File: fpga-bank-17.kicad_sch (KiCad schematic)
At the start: 1 part, among them U1 XC7K410T-2FFG900I

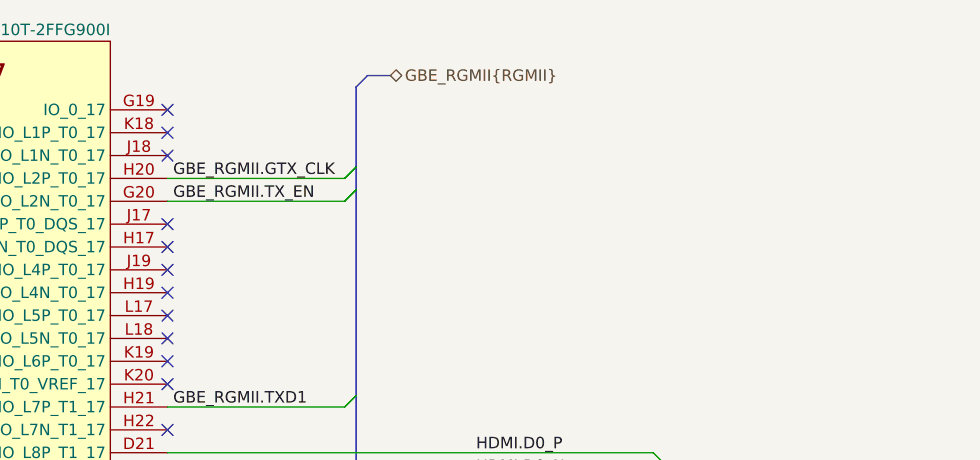
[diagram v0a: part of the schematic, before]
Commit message: Added control signals on FMC connector
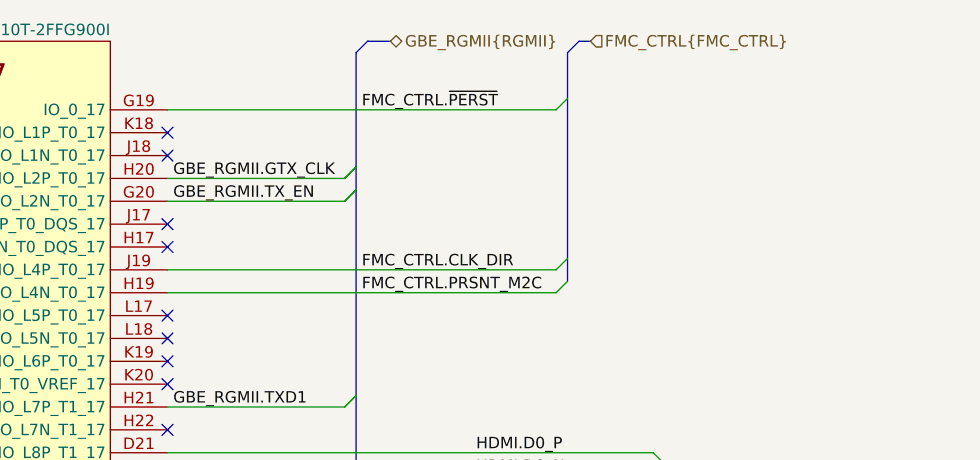
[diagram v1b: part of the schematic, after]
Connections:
- net FMC_CTRL.~{PERST}: now reaches U1.G19 (IO_0_17)
- net FMC_CTRL.PRSNT_M2C: now reaches U1.H19 (IO_L4N_T0_17)
- net FMC_CTRL.CLK_DIR: now reaches U1.J19 (IO_L4P_T0_17)
- no-connect marks 18 -> 15
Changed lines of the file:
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@@
   (no_connect (at 143.51 109.22))
   (no_connect (at 143.51 99.06))
-  (no_connect (at 143.51 101.6))
-  (no_connect (at 143.51 104.14))
   (no_connect (at 143.51 106.68))
   (no_connect (at 143.51 96.52))
-  (no_connect (at 143.51 83.82))
   (no_connect (at 143.51 86.36))
   (no_connect (at 143.51 88.9))
@@
     (stroke (width 0) (type default) (color 0 0 0 0))
   )
+  (bus_entry (at 187.96 82.55) (size -1.27 1.27)
+    (stroke (width 0) (type default) (color 0 0 0 0))
+  )
   (bus_entry (at 164.465 133.35) (size -1.27 1.27)
     (stroke (width 0) (type default) (color 0 0 0 0))
@@
     (stroke (width 0) (type default) (color 0 0 0 0))
   )
+  (bus_entry (at 187.96 102.87) (size -1.27 1.27)
+    (stroke (width 0) (type default) (color 0 0 0 0))
+  )
   (bus_entry (at 231.14 166.37) (size -1.27 1.27)
     (stroke (width 0) (type default) (color 0 0 0 0))
@@
     (stroke (width 0) (type default) (color 0 0 0 0))
   )
+  (bus_entry (at 187.96 100.33) (size -1.27 1.27)
+    (stroke (width 0) (type default) (color 0 0 0 0))
+  )
   (bus_entry (at 197.485 177.8) (size 1.27 1.27)
     (stroke (width 0) (type default) (color 0 0 0 0))
@@
     (stroke (width 0) (type default) (color 0 0 0 0))
   )
-  (bus (pts (xy 164.465 81.28) (xy 164.465 90.17))
-    (stroke (width 0) (type default) (color 0 0 0 0))
-  )
-  (bus (pts (xy 168.275 80.01) (xy 165.735 80.01))
+  (bus (pts (xy 187.96 82.55) (xy 187.96 100.33))
+    (stroke (width 0) (type default) (color 0 0 0 0))
+  )
+  (bus (pts (xy 164.465 77.47) (xy 164.465 90.17))
+    (stroke (width 0) (type default) (color 0 0 0 0))
+  )
+  (bus (pts (xy 168.275 76.2) (xy 165.735 76.2))
     (stroke (width 0) (type default) (color 0 0 0 0))
   )
@@
     (stroke (width 0) (type default) (color 0 0 0 0))
   )
-  (bus (pts (xy 164.465 81.28) (xy 165.735 80.01))
+  (bus (pts (xy 164.465 77.47) (xy 165.735 76.2))
+    (stroke (width 0) (type default) (color 0 0 0 0))
+  )
+  (wire (pts (xy 143.51 83.82) (xy 186.69 83.82))
     (stroke (width 0) (type default) (color 0 0 0 0))
   )
@@
     (stroke (width 0) (type default) (color 0 0 0 0))
   )
+  (bus (pts (xy 190.5 76.2) (xy 189.23 76.2))
+    (stroke (width 0) (type default) (color 0 0 0 0))
+  )
   (wire (pts (xy 143.51 185.42) (xy 229.87 185.42))
     (stroke (width 0) (type default) (color 0 0 0 0))
@@
     (stroke (width 0) (type default) (color 0 0 0 0))
   )
+  (bus (pts (xy 187.96 100.33) (xy 187.96 102.87))
+    (stroke (width 0) (type default) (color 0 0 0 0))
+  )
   (wire (pts (xy 143.51 195.58) (xy 229.87 195.58))
     (stroke (width 0) (type default) (color 0 0 0 0))
@@
     (stroke (width 0) (type default) (color 0 0 0 0))
   )
+  (bus (pts (xy 187.96 77.47) (xy 187.96 82.55))
+    (stroke (width 0) (type default) (color 0 0 0 0))
+  )
+  (bus (pts (xy 187.96 77.47) (xy 189.23 76.2))
+    (stroke (width 0) (type default) (color 0 0 0 0))
+  )
   (bus (pts (xy 198.755 207.01) (xy 198.755 208.915))
     (stroke (width 0) (type default) (color 0 0 0 0))
@@
     (stroke (width 0) (type default) (color 0 0 0 0))
   )
+  (wire (pts (xy 143.51 104.14) (xy 186.69 104.14))
+    (stroke (width 0) (type default) (color 0 0 0 0))
+  )
   (wire (pts (xy 197.485 203.2) (xy 143.51 203.2))
     (stroke (width 0) (type default) (color 0 0 0 0))
@@
   )
   (wire (pts (xy 143.51 170.18) (xy 229.87 170.18))
+    (stroke (width 0) (type default) (color 0 0 0 0))
+  )
+  (wire (pts (xy 143.51 101.6) (xy 186.69 101.6))
     (stroke (width 0) (type default) (color 0 0 0 0))
   )
@@
     (effects (font (size 1.27 1.27)) (justify left bottom))
   )
+  (label "FMC_CTRL.PRSNT_M2C" (at 165.1 104.14 0)
+    (effects (font (size 1.27 1.27)) (justify left bottom))
+  )
   (label "HDMI.D2_N" (at 177.8 205.74 0)
     (effects (font (size 1.27 1.27)) (justify left bottom))
@@
     (effects (font (size 1.27 1.27)) (justify left bottom))
   )
+  (label "FMC_CTRL.CLK_DIR" (at 165.1 101.6 0)
+    (effects (font (size 1.27 1.27)) (justify left bottom))
+  )
   (label "GBE_RGMII.REFCLK" (at 144.145 162.56 0)
     (effects (font (size 1.27 1.27)) (justify left bottom))
   )
+  (label "FMC_CTRL.~{PERST}" (at 165.1 83.82 0)
+    (effects (font (size 1.27 1.27)) (justify left bottom))
+  )
   (label "GBE_RGMII.RXD1" (at 144.145 157.48 0)
     (effects (font (size 1.27 1.27)) (justify left bottom))
   )
-  (hierarchical_label "GBE_RGMII{RGMII}" (shape bidirectional) (at 168.275 80.01 0)
+  (hierarchical_label "GBE_RGMII{RGMII}" (shape bidirectional) (at 168.275 76.2 0)
     (effects (font (size 1.27 1.27)) (justify left))
   )
@@
     (effects (font (size 1.27 1.27)) (justify left))
   )
+  (hierarchical_label "FMC_CTRL{FMC_CTRL}" (shape input) (at 190.5 76.2 0)
+    (effects (font (size 1.27 1.27)) (justify left))
+  )

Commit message: Bump revision to 1.0.0. Update name on schematic and PCB sheets
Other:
- title: K410T devboard -> Kintex 410T devboard

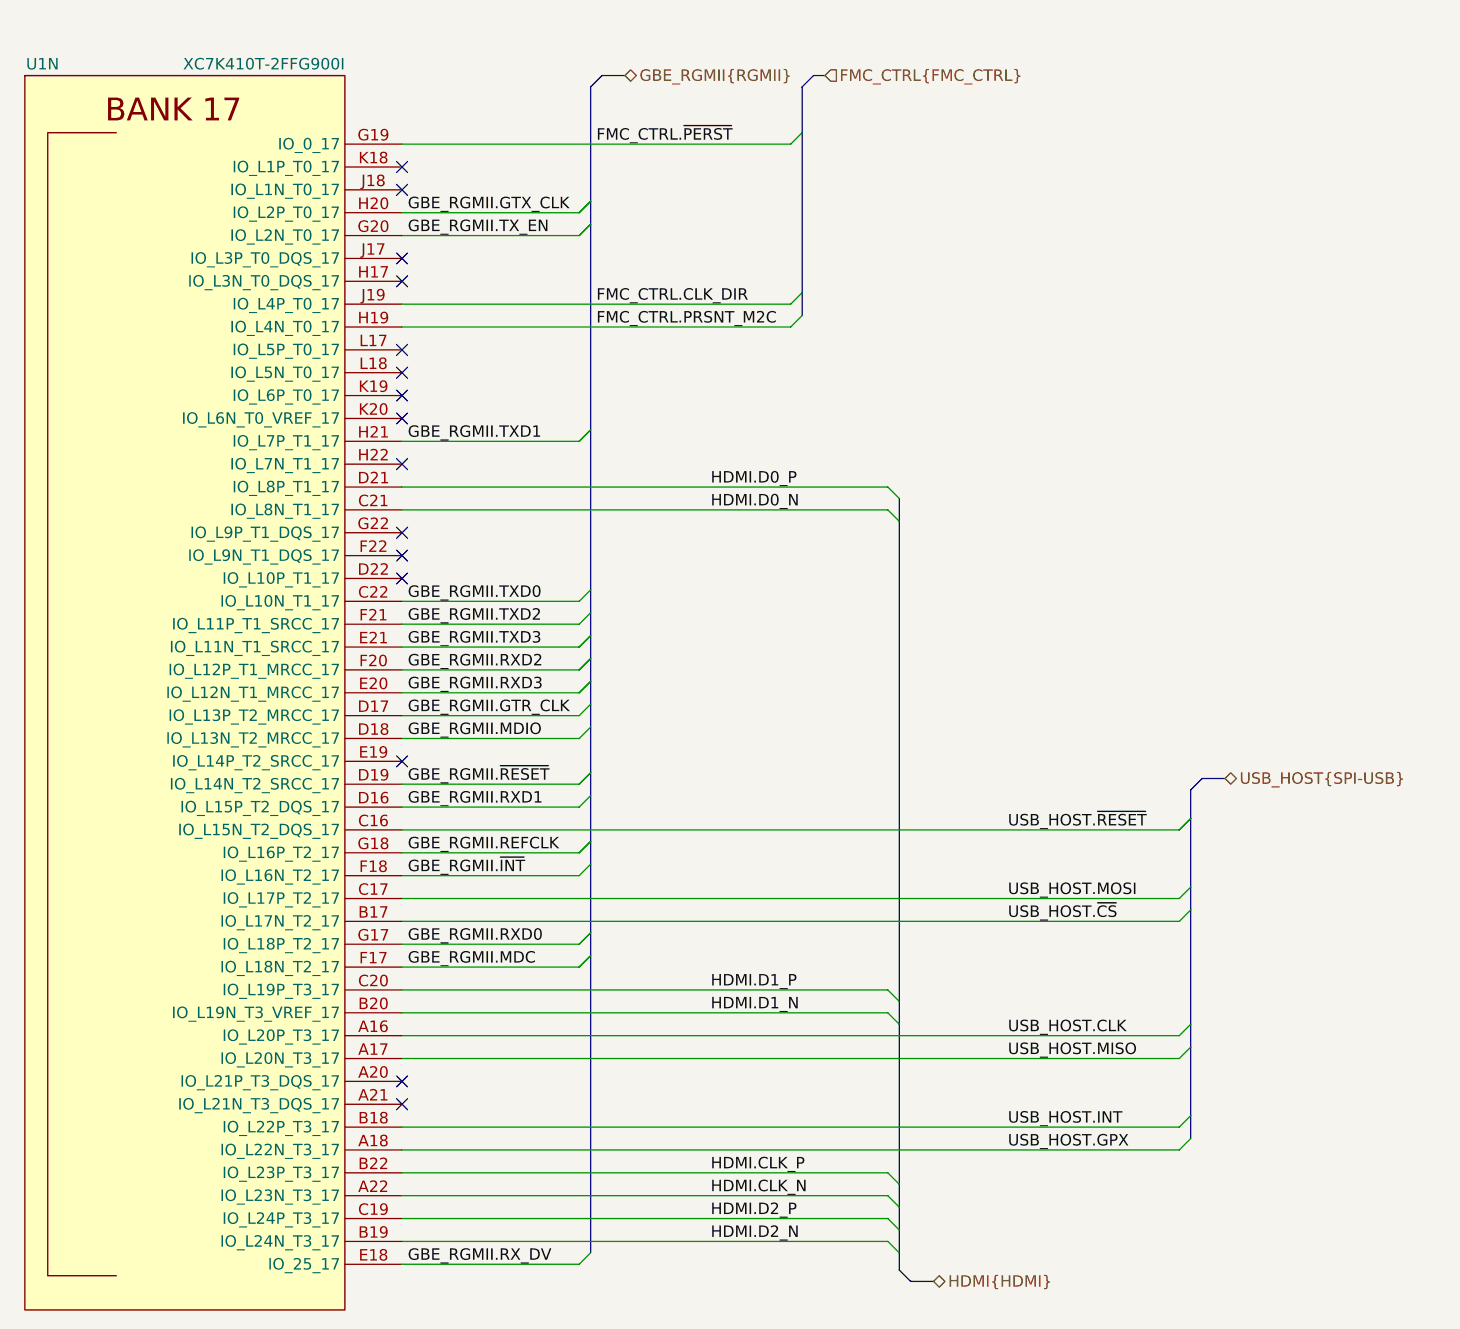
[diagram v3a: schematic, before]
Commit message: Introduce component standardization
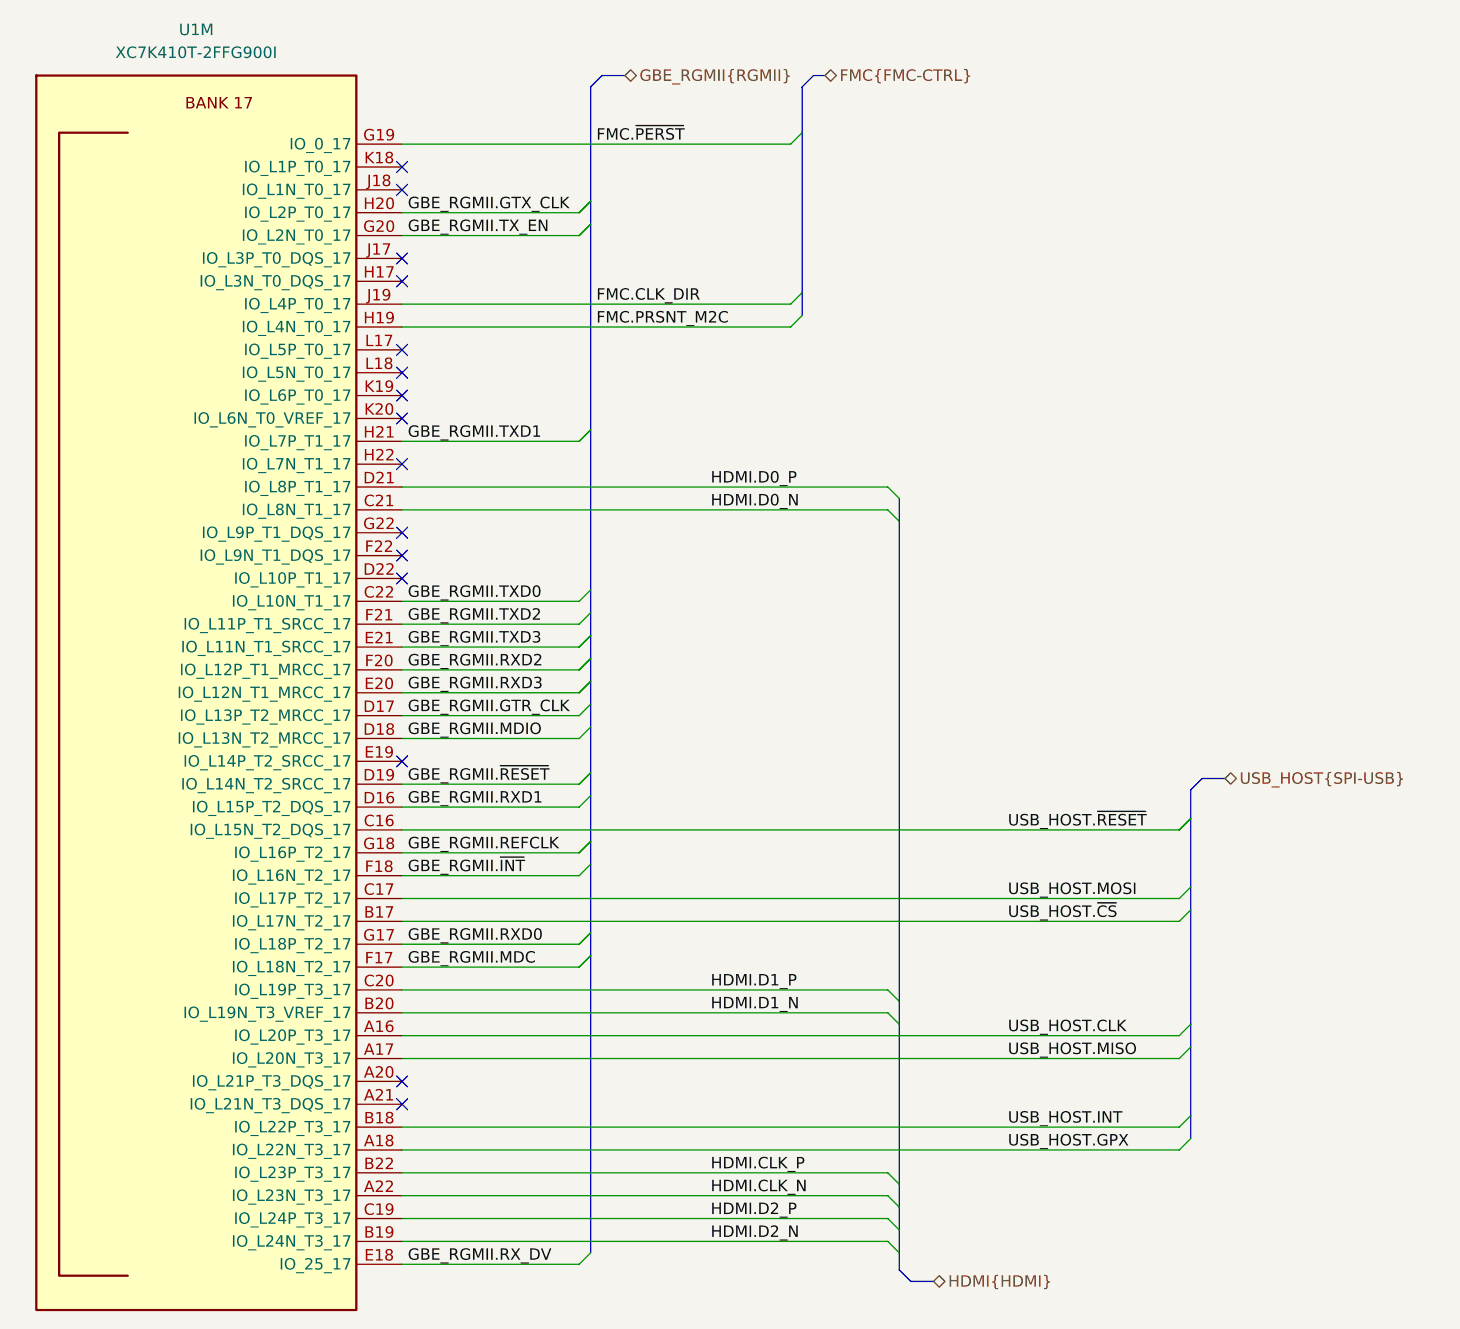
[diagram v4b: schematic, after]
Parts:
- removed U1: XC7K410T-2FFG900I, K410T-devboard-footprints:xc7k410t-2ffg900I, symbol K410T-devboard:XC7K410T-2FFG900I
- added U1: XC7K410T-2FFG900I, K410T-devboard-footprints:xc7k410t-2ffg900I, symbol K410T-devboard:XC7K410T-2FFG900I
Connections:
- net GBE_RGMII.GTR_CLK: now also U1.D17 (IO_L13P_T2_MRCC_17)
- net GBE_RGMII.GTX_CLK: now also U1.H20 (IO_L2P_T0_17)
- net GBE_RGMII.MDC: now also U1.F17 (IO_L18N_T2_17)
- net GBE_RGMII.MDIO: now also U1.D18 (IO_L13N_T2_MRCC_17)
- net GBE_RGMII.REFCLK: now also U1.G18 (IO_L16P_T2_17)
- net GBE_RGMII.RXD0: now also U1.G17 (IO_L18P_T2_17)
- net GBE_RGMII.RXD1: now also U1.D16 (IO_L15P_T2_DQS_17)
- net GBE_RGMII.RXD2: now also U1.F20 (IO_L12P_T1_MRCC_17)
- net GBE_RGMII.RXD3: now also U1.E20 (IO_L12N_T1_MRCC_17)
- net GBE_RGMII.RX_DV: now also U1.E18 (IO_25_17)
- net GBE_RGMII.TXD0: now also U1.C22 (IO_L10N_T1_17)
- net GBE_RGMII.TXD1: now also U1.H21 (IO_L7P_T1_17)
- net GBE_RGMII.TXD2: now also U1.F21 (IO_L11P_T1_SRCC_17)
- net GBE_RGMII.TXD3: now also U1.E21 (IO_L11N_T1_SRCC_17)
- net GBE_RGMII.TX_EN: now also U1.G20 (IO_L2N_T0_17)
- net GBE_RGMII.~{INT}: now also U1.F18 (IO_L16N_T2_17)
- net GBE_RGMII.~{RESET}: now also U1.D19 (IO_L14N_T2_SRCC_17)
- net HDMI.CLK_N: now also U1.A22 (IO_L23N_T3_17)
- net HDMI.CLK_P: now also U1.B22 (IO_L23P_T3_17)
- net HDMI.D0_N: now also U1.C21 (IO_L8N_T1_17)
- net HDMI.D0_P: now also U1.D21 (IO_L8P_T1_17)
- net HDMI.D1_N: now also U1.B20 (IO_L19N_T3_VREF_17)
- net HDMI.D1_P: now also U1.C20 (IO_L19P_T3_17)
- net HDMI.D2_N: now also U1.B19 (IO_L24N_T3_17)
- net HDMI.D2_P: now also U1.C19 (IO_L24P_T3_17)
- net USB_HOST.CLK: now also U1.A16 (IO_L20P_T3_17)
- net USB_HOST.GPX: now also U1.A18 (IO_L22N_T3_17)
- net USB_HOST.INT: now also U1.B18 (IO_L22P_T3_17)
- net USB_HOST.MISO: now also U1.A17 (IO_L20N_T3_17)
- net USB_HOST.MOSI: now also U1.C17 (IO_L17P_T2_17)
- net USB_HOST.~{CS}: now also U1.B17 (IO_L17N_T2_17)
- net USB_HOST.~{RESET}: now also U1.C16 (IO_L15N_T2_DQS_17)
- new net FMC.CLK_DIR: U1.J19 (IO_L4P_T0_17)
- new net FMC.PRSNT_M2C: U1.H19 (IO_L4N_T0_17)
- new net FMC.~{PERST}: U1.G19 (IO_0_17)
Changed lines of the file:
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@@
     (title "Kintex 410T devboard")
     (date "2023-02-01")
-    (rev "1.0.0")
+    (rev "1.1.1")
   )
   (no_connect (at 143.51 152.4))
@@
     (effects (font (size 1.27 1.27)) (justify left bottom))
   )
-  (label "FMC_CTRL.PRSNT_M2C" (at 165.1 104.14 0)
+  (label "FMC.PRSNT_M2C" (at 165.1 104.14 0)
     (effects (font (size 1.27 1.27)) (justify left bottom))
   )
@@
     (effects (font (size 1.27 1.27)) (justify left bottom))
   )
-  (label "FMC_CTRL.CLK_DIR" (at 165.1 101.6 0)
+  (label "FMC.CLK_DIR" (at 165.1 101.6 0)
     (effects (font (size 1.27 1.27)) (justify left bottom))
   )
@@
     (effects (font (size 1.27 1.27)) (justify left bottom))
   )
-  (label "FMC_CTRL.~{PERST}" (at 165.1 83.82 0)
+  (label "FMC.~{PERST}" (at 165.1 83.82 0)
     (effects (font (size 1.27 1.27)) (justify left bottom))
   )
@@
     (effects (font (size 1.27 1.27)) (justify left))
   )
-  (hierarchical_label "FMC_CTRL{FMC_CTRL}" (shape input) (at 190.5 76.2 0)
+  (hierarchical_label "FMC{FMC-CTRL}" (shape bidirectional) (at 190.5 76.2 0)
     (effects (font (size 1.27 1.27)) (justify left))
   )
-  (symbol (lib_id "K410T-devboard:XC7K410T-2FFG900I") (at 119.38 144.78 0) (unit 14)
-    (in_bom yes) (on_board yes)
-    (property "Reference" "U1" (id 0) (at 105.41 74.93 0)
-      (effects (font (size 1.27 1.27)) (justify right))
+  (symbol (lib_id "K410T-devboard:XC7K410T-2FFG900I") (at 143.51 83.82 0) (unit 13)
+    (in_bom yes) (on_board yes) (fields_autoplaced)
+    (property "Reference" "U1" (id 0) (at 120.65 71.12 0)
+      (effects (font (size 1.27 1.27) (thickness 0.15)))
     )
-    (property "Value" "XC7K410T-2FFG900I" (id 1) (at 137.16 74.93 0)
-      (effects (font (size 1.27 1.27)) (justify right))
+    (property "Value" "XC7K410T-2FFG900I" (id 1) (at 120.65 73.66 0)
+      (effects (font (size 1.27 1.27) (thickness 0.15)))
     )
-    (property "Footprint" "K410T-devboard-footprints:xc7k410t-2ffg900I" (id 2) (at 119.38 219.71 0)
-      (effects (font (size 1.27 1.27)) hide)
+    (property "Footprint" "K410T-devboard-footprints:xc7k410t-2ffg900I" (id 2) (at 143.51 57.15 0)
+      (effects (font (size 1.27 1.27) (thickness 0.15)) (justify left bottom) hide)
     )
-    (property "Datasheet" "https://eu.mouser.com/datasheet/2/903/ds180_7Series_Overview-1591537.pdf" (id 3) (at 119.38 222.25 0)
-      (effects (font (size 1.27 1.27)) hide)
+    (property "Datasheet" "https://eu.mouser.com/datasheet/2/903/ds180_7Series_Overview-1591537.pdf" (id 3) (at 143.51 59.69 0)
+      (effects (font (size 1.27 1.27) (thickness 0.15)) (justify left bottom) hide)
     )
-    (property "Manufacturer" "Xilinx" (id 4) (at 119.38 214.63 0)
-      (effects (font (size 1.27 1.27)) hide)
+    (property "Manufacturer" "Xilinx" (id 4) (at 143.51 62.23 0)
+      (effects (font (size 1.27 1.27) (thickness 0.15)) (justify left bottom) hide)
     )
-    (property "MPN" "XC7K410T-2FFG900I" (id 5) (at 119.38 217.17 0)
-      (effects (font (size 1.27 1.27)) hide)
+    (property "MPN" "XC7K410T-2FFG900I" (id 5) (at 143.51 64.77 0)
+      (effects (font (size 1.27 1.27) (thickness 0.15)) (justify left bottom) hide)
+    )
+    (property "Author" "Antmicro" (id 6) (at 143.51 67.31 0)
+      (effects (font (size 1.27 1.27) (thickness 0.15)) (justify left bottom) hide)
+    )
+    (property "License" "Apache-2.0" (id 7) (at 143.51 69.85 0)
+      (effects (font (size 1.27 1.27) (thickness 0.15)) (justify left bottom) hide)
     )
     (pin "AA20")
@@
     (pin "Y12")
     (pin "Y22")
-    (pin "C10")
-    (pin "M11")
-    (pin "M13")
-    (pin "M15")
-    (pin "M17")
-    (pin "N10")
-    (pin "N12")
-    (pin "N14")
-    (pin "N16")
-    (pin "N18")
-    (pin "P11")
-    (pin "P13")
-    (pin "P14")
-    (pin "P15")
-    (pin "P17")
-    (pin "R10")
-    (pin "R12")
-    (pin "R16")
-    (pin "R18")
-    (pin "T11")
-    (pin "T13")
-    (pin "T17")
-    (pin "U10")
-    (pin "U12")
-    (pin "U16")
-    (pin "U18")
-    (pin "V11")
-    (pin "V13")
-    (pin "V15")
-    (pin "V17")
-    (pin "W10")
-    (pin "W12")
-    (pin "W14")
-    (pin "W16")
-    (pin "W18")
     (pin "A1")
     (pin "A14")
@@
     (pin "B9")
     (pin "C1")
+    (pin "C10")
     (pin "C18")
     (pin "C2")
@@
     (pin "L6")
     (pin "L9")
+    (pin "M11")
     (pin "M12")
+    (pin "M13")
     (pin "M14")
+    (pin "M15")
     (pin "M16")
+    (pin "M17")
     (pin "M18")
     (pin "M21")
@@
     (pin "M9")
     (pin "N1")
+    (pin "N10")
     (pin "N11")
+    (pin "N12")
     (pin "N13")
+    (pin "N14")
     (pin "N15")
+    (pin "N16")
     (pin "N17")
+    (pin "N18")
     (pin "N2")
     (pin "N28")
@@
     (pin "N9")
     (pin "P10")
+    (pin "P11")
     (pin "P12")
+    (pin "P13")
+    (pin "P14")
+    (pin "P15")
     (pin "P16")
+    (pin "P17")
     (pin "P18")
     (pin "P25")
@@
     (pin "P9")
     (pin "R1")
+    (pin "R10")
     (pin "R11")
+    (pin "R12")
     (pin "R13")
+    (pin "R16")
     (pin "R17")
+    (pin "R18")
     (pin "R2")
     (pin "R22")
@@
     (pin "R9")
     (pin "T10")
+    (pin "T11")
     (pin "T12")
+    (pin "T13")
     (pin "T16")
+    (pin "T17")
     (pin "T18")
     (pin "T19")
@@
     (pin "T8")
     (pin "U1")
+    (pin "U10")
     (pin "U11")
+    (pin "U12")
     (pin "U13")
+    (pin "U16")
     (pin "U17")
+    (pin "U18")
     (pin "U2")
     (pin "U26")
@@
     (pin "U9")
     (pin "V10")
+    (pin "V11")
     (pin "V12")
+    (pin "V13")
     (pin "V14")
+    (pin "V15")
     (pin "V16")
+    (pin "V17")
     (pin "V18")
     (pin "V23")
@@
     (pin "V9")
     (pin "W1")
+    (pin "W10")
     (pin "W11")
+    (pin "W12")
     (pin "W13")
+    (pin "W14")
     (pin "W15")
+    (pin "W16")
     (pin "W17")
+    (pin "W18")
     (pin "W2")
     (pin "W20")
